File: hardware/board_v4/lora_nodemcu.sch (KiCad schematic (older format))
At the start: 13 parts, among them J1 Solar Panel, J2 LiPo 18650, J6 RF_Shield_ESP-07S, J7 RF_Shield_RFM95

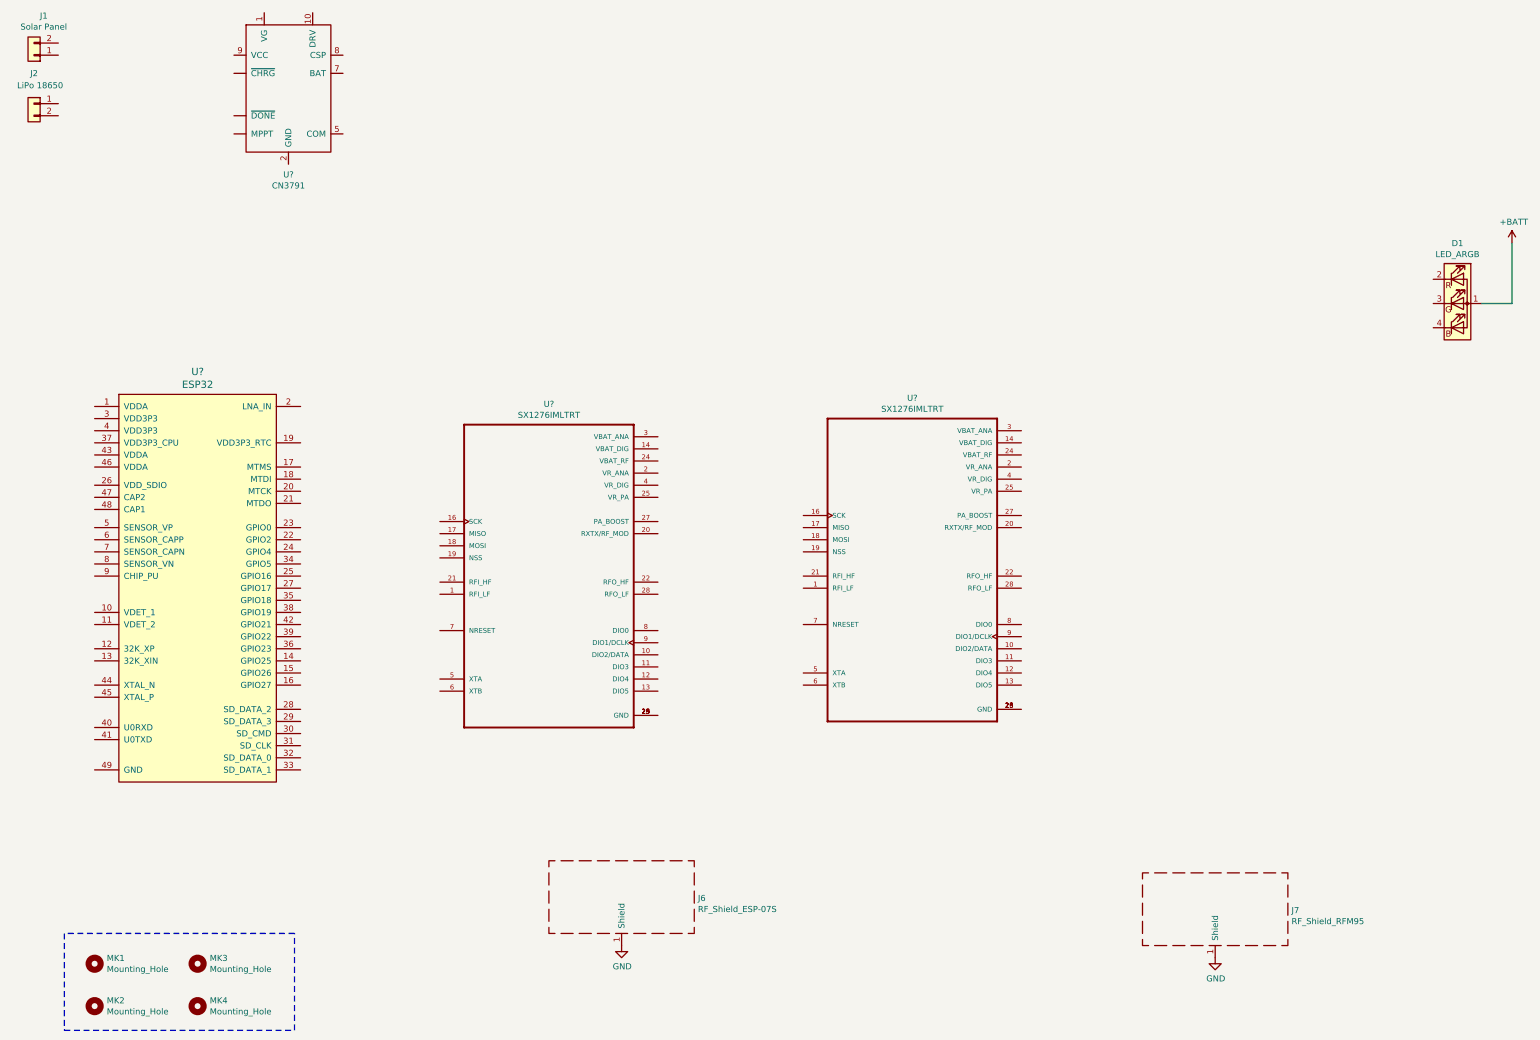
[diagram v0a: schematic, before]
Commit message: adds new ESP32 board
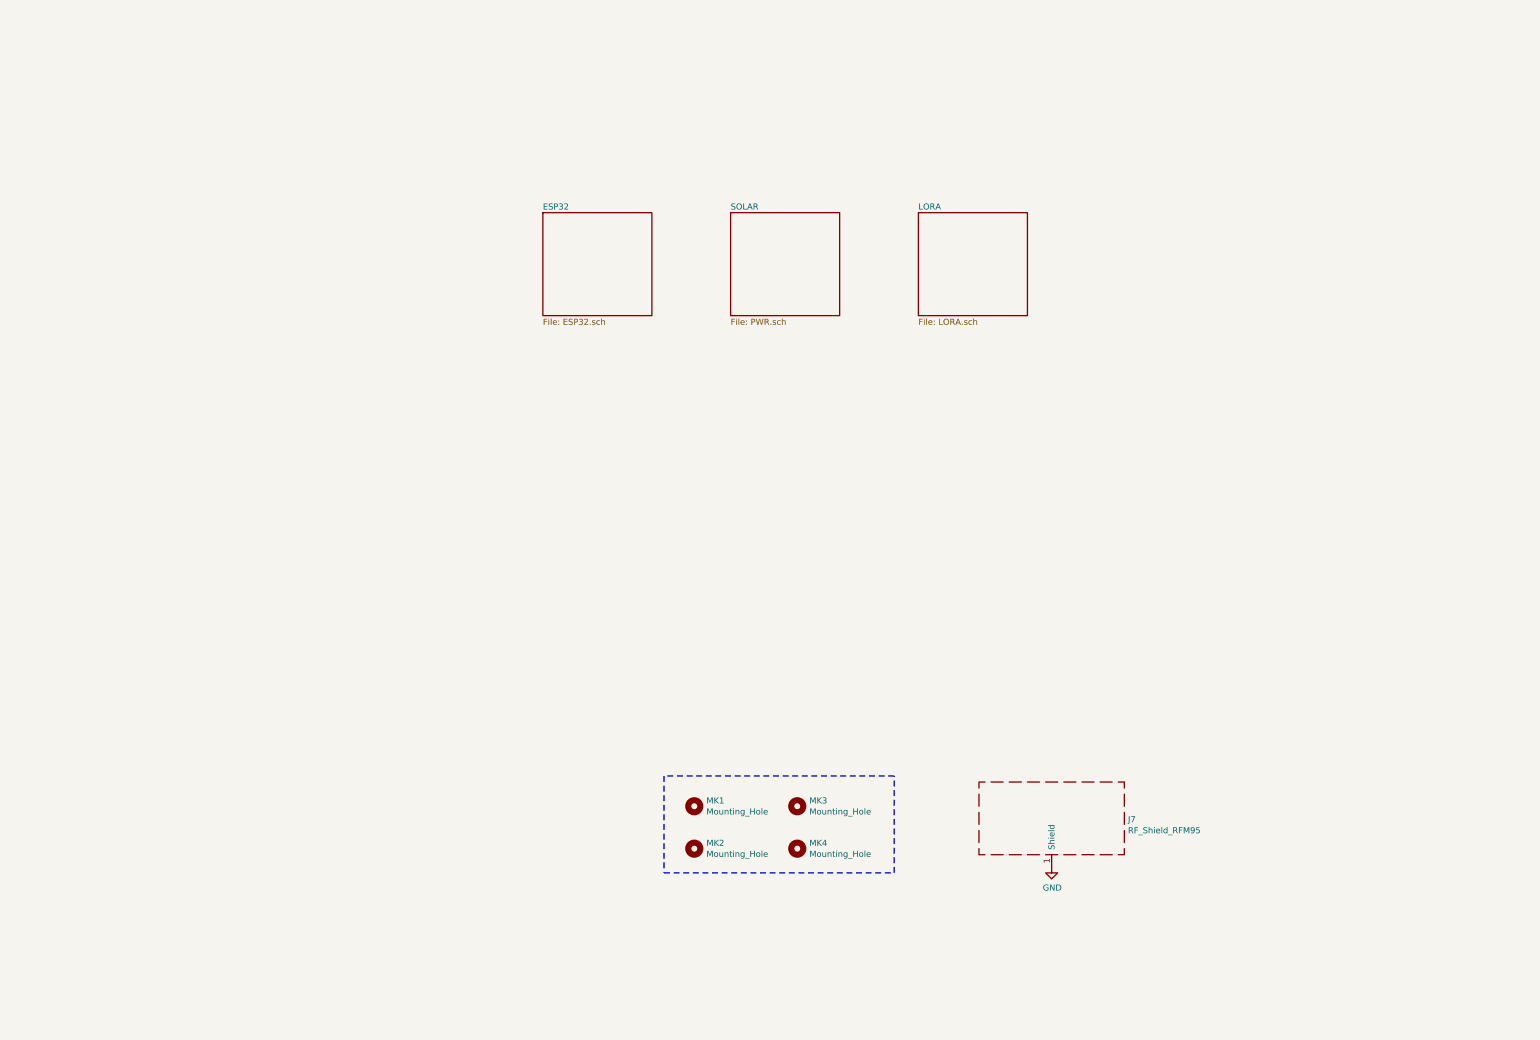
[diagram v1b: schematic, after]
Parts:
- removed D1: LED_ARGB, LED_THT:LED_D5.0mm-4, symbol Device:LED_ARGB
- removed J1: Solar Panel, disaster_radio:solar_panel_conn, symbol Connector_Generic:Conn_01x02
- removed J2: LiPo 18650, Battery:BatteryHolder_MPD_BH-18650-PC2, symbol Connector_Generic:Conn_01x02
- removed J6: RF_Shield_ESP-07S, RF_Shielding:Wuerth_36103305_30x30mm, symbol Device:RF_Shield_One_Piece
- removed U?: CN3791, symbol disaster_radio:CN3791
- removed U?: ESP32, ESP32-footprints-Lib:ESP32, symbol disaster_radio:ESP32
- removed U? (x2): SX1276IMLTRT, QFN65P600X600X100-29N, symbol disaster_radio:SX1276IMLTRT
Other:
- moved on the sheet: J7, MK1, MK2, MK3, MK4
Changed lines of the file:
@@
 EESchema Schematic File Version 4
 LIBS:lora_nodemcu-cache
-EELAYER 26 0
+EELAYER 29 0
 EELAYER END
 $Descr A3 16535 11693
 encoding utf-8
-Sheet 1 1
+Sheet 1 4
 Title ""
 Date ""
@@
 $EndDescr
 $Comp
-L Connector_Generic:Conn_01x02 J2
-U 1 1 5AA4CAA2
-P 1350 1850
-F 0 "J2" H 1350 2100 50  0000 C CNN
-F 1 "LiPo 18650" H 1300 2000 50  0000 C CNN
-F 2 "Battery:BatteryHolder_MPD_BH-18650-PC2" H 1350 1850 50  0001 C CNN
-F 3 "~" H 1350 1850 50  0001 C CNN
-	1    1350 1850
-	-1   0    0    -1
-$EndComp
-$Comp
-L Connector_Generic:Conn_01x02 J1
-U 1 1 5AA4DEE1
-P 1350 1450
-F 0 "J1" H 1270 1125 50  0000 C CNN
-F 1 "Solar Panel" H 1270 1216 50  0000 C CNN
-F 2 "disaster_radio:solar_panel_conn" H 1350 1450 50  0001 C CNN
-F 3 "~" H 1350 1450 50  0001 C CNN
-	1    1350 1450
-	-1   0    0    1
-$EndComp
-$Comp
-L power:+BATT #PWR0125
-U 1 1 5ADE71D1
-P 13550 3000
-F 0 "#PWR0125" H 13550 2850 50  0001 C CNN
-F 1 "+BATT" H 13565 3173 50  0000 C CNN
-F 2 "" H 13550 3000 50  0001 C CNN
-F 3 "" H 13550 3000 50  0001 C CNN
-	1    13550 3000
-	1    0    0    -1
-$EndComp
-Wire Wire Line
-	13550 3000 13550 3500
-$Comp
 L lora_nodemcu-rescue:Mounting_Hole-Mechanical MK1
 U 1 1 5ABC6521
-P 1850 8950
-F 0 "MK1" H 1950 8996 50  0000 L CNN
-F 1 "Mounting_Hole" H 1950 8905 50  0000 L CNN
-F 2 "MountingHole:MountingHole_3.2mm_M3" H 1850 8950 50  0001 C CNN
-F 3 "" H 1850 8950 50  0001 C CNN
-	1    1850 8950
+P 6800 7650
+F 0 "MK1" H 6900 7696 50  0000 L CNN
+F 1 "Mounting_Hole" H 6900 7605 50  0000 L CNN
+F 2 "MountingHole:MountingHole_3.2mm_M3" H 6800 7650 50  0001 C CNN
+F 3 "" H 6800 7650 50  0001 C CNN
+	1    6800 7650
 	1    0    0    -1
 $EndComp
@@
 L lora_nodemcu-rescue:Mounting_Hole-Mechanical MK3
 U 1 1 5ABC68A6
-P 2700 8950
-F 0 "MK3" H 2800 8996 50  0000 L CNN
-F 1 "Mounting_Hole" H 2800 8905 50  0000 L CNN
-F 2 "MountingHole:MountingHole_3.2mm_M3" H 2700 8950 50  0001 C CNN
-F 3 "" H 2700 8950 50  0001 C CNN
-	1    2700 8950
+P 7650 7650
+F 0 "MK3" H 7750 7696 50  0000 L CNN
+F 1 "Mounting_Hole" H 7750 7605 50  0000 L CNN
+F 2 "MountingHole:MountingHole_3.2mm_M3" H 7650 7650 50  0001 C CNN
+F 3 "" H 7650 7650 50  0001 C CNN
+	1    7650 7650
 	1    0    0    -1
 $EndComp
@@
 L lora_nodemcu-rescue:Mounting_Hole-Mechanical MK2
 U 1 1 5ABC6A8E
-P 1850 9300
-F 0 "MK2" H 1950 9346 50  0000 L CNN
-F 1 "Mounting_Hole" H 1950 9255 50  0000 L CNN
-F 2 "MountingHole:MountingHole_3.2mm_M3" H 1850 9300 50  0001 C CNN
-F 3 "" H 1850 9300 50  0001 C CNN
-	1    1850 9300
+P 6800 8000
+F 0 "MK2" H 6900 8046 50  0000 L CNN
+F 1 "Mounting_Hole" H 6900 7955 50  0000 L CNN
+F 2 "MountingHole:MountingHole_3.2mm_M3" H 6800 8000 50  0001 C CNN
+F 3 "" H 6800 8000 50  0001 C CNN
+	1    6800 8000
 	1    0    0    -1
 $EndComp
@@
 L lora_nodemcu-rescue:Mounting_Hole-Mechanical MK4
 U 1 1 5ABC6A95
-P 2700 9300
-F 0 "MK4" H 2800 9346 50  0000 L CNN
-F 1 "Mounting_Hole" H 2800 9255 50  0000 L CNN
-F 2 "MountingHole:MountingHole_3.2mm_M3" H 2700 9300 50  0001 C CNN
-F 3 "" H 2700 9300 50  0001 C CNN
-	1    2700 9300
+P 7650 8000
+F 0 "MK4" H 7750 8046 50  0000 L CNN
+F 1 "Mounting_Hole" H 7750 7955 50  0000 L CNN
+F 2 "MountingHole:MountingHole_3.2mm_M3" H 7650 8000 50  0001 C CNN
+F 3 "" H 7650 8000 50  0001 C CNN
+	1    7650 8000
 	1    0    0    -1
 $EndComp
-$Comp
-L Device:LED_ARGB D1
-U 1 1 5ABCE072
-P 13100 3500
-F 0 "D1" H 13100 3997 50  0000 C CNN
-F 1 "LED_ARGB" H 13100 3906 50  0000 C CNN
-F 2 "LED_THT:LED_D5.0mm-4" H 13100 3450 50  0001 C CNN
-F 3 "~" H 13100 3450 50  0001 C CNN
-	1    13100 3500
-	1    0    0    -1
-$EndComp
-Wire Wire Line
-	13300 3500 13550 3500
 Wire Notes Line
-	1600 8700 1600 9500
+	6550 7400 6550 8200
 Wire Notes Line
-	1600 9500 3500 9500
+	6550 8200 8450 8200
 Wire Notes Line
-	3500 9500 3500 8700
+	8450 8200 8450 7400
 Wire Notes Line
-	3500 8700 1600 8700
-$Comp
-L disaster_radio:CN3791 U?
-U 1 1 5BEC3801
-P 3450 1700
-F 0 "U?" H 3450 964 50  0000 C CNN
-F 1 "CN3791" H 3450 873 50  0000 C CNN
-F 2 "" H 3450 1700 50  0001 C CNN
-F 3 "" H 3450 1700 50  0001 C CNN
-	1    3450 1700
-	1    0    0    -1
-$EndComp
-$Comp
-L disaster_radio:ESP32 U?
-U 1 1 5BEE2399
-P 2700 5900
-F 0 "U?" H 2700 7737 60  0000 C CNN
-F 1 "ESP32" H 2700 7631 60  0000 C CNN
-F 2 "ESP32-footprints-Lib:ESP32" H 2700 4275 60  0001 C CNN
-F 3 "" H 3150 6800 60  0001 C CNN
-	1    2700 5900
-	1    0    0    -1
-$EndComp
-$Comp
-L power:GND #PWR0128
-U 1 1 5AB442E3
-P 6200 8800
-F 0 "#PWR0128" H 6200 8550 50  0001 C CNN
-F 1 "GND" H 6205 8627 50  0000 C CNN
-F 2 "" H 6200 8800 50  0001 C CNN
-F 3 "" H 6200 8800 50  0001 C CNN
-	1    6200 8800
-	1    0    0    -1
-$EndComp
-$Comp
-L Device:RF_Shield_One_Piece J6
-U 1 1 5AB442DC
-P 6200 8400
-F 0 "J6" H 6830 8391 50  0000 L CNN
-F 1 "RF_Shield_ESP-07S" H 6830 8300 50  0000 L CNN
-F 2 "RF_Shielding:Wuerth_36103305_30x30mm" H 6200 8300 50  0001 C CNN
-F 3 "~" H 6200 8300 50  0001 C CNN
-	1    6200 8400
-	1    0    0    -1
-$EndComp
+	8450 7400 6550 7400
 $Comp
 L power:GND #PWR0127
 U 1 1 5AB4404A
-P 11100 8900
-F 0 "#PWR0127" H 11100 8650 50  0001 C CNN
-F 1 "GND" H 11105 8727 50  0000 C CNN
-F 2 "" H 11100 8900 50  0001 C CNN
-F 3 "" H 11100 8900 50  0001 C CNN
-	1    11100 8900
+P 9750 8150
+F 0 "#PWR0127" H 9750 7900 50  0001 C CNN
+F 1 "GND" H 9755 7977 50  0000 C CNN
+F 2 "" H 9750 8150 50  0001 C CNN
+F 3 "" H 9750 8150 50  0001 C CNN
+	1    9750 8150
 	1    0    0    -1
 $EndComp
@@
 L Device:RF_Shield_One_Piece J7
 U 1 1 5AB43EB6
-P 11100 8500
-F 0 "J7" H 11730 8491 50  0000 L CNN
-F 1 "RF_Shield_RFM95" H 11730 8400 50  0000 L CNN
-F 2 "RF_Shielding:Wuerth_36103305_30x30mm" H 11100 8400 50  0001 C CNN
-F 3 "~" H 11100 8400 50  0001 C CNN
-	1    11100 8500
+P 9750 7750
+F 0 "J7" H 10380 7741 50  0000 L CNN
+F 1 "RF_Shield_RFM95" H 10380 7650 50  0000 L CNN
+F 2 "RF_Shielding:Wuerth_36103305_30x30mm" H 9750 7650 50  0001 C CNN
+F 3 "~" H 9750 7650 50  0001 C CNN
+	1    9750 7750
 	1    0    0    -1
 $EndComp
-$Comp
-L disaster_radio:SX1276IMLTRT U?
-U 1 1 5BEE32F7
-P 5600 5800
-F 0 "U?" H 5600 7270 50  0000 C CNN
-F 1 "SX1276IMLTRT" H 5600 7179 50  0000 C CNN
-F 2 "QFN65P600X600X100-29N" H 5600 5800 50  0001 L BNN
-F 3 "SX1276IMLTRT" H 5600 5800 50  0001 L BNN
-F 4 "None" H 5600 5800 50  0001 L BNN "Field4"
-F 5 "Rf Ism Transceiver Fsk/gfsk/gmsk/msk/ook 3.3V Automotive 28-PIN QFN Ep T/r" H 5600 5800 50  0001 L BNN "Field5"
-F 6 "Unavailable" H 5600 5800 50  0001 L BNN "Field6"
-F 7 "VQFN-28 Semtech" H 5600 5800 50  0001 L BNN "Field7"
-F 8 "Semtech Corporation" H 5600 5800 50  0001 L BNN "Field8"
-	1    5600 5800
-	1    0    0    -1
-$EndComp
-$Comp
-L disaster_radio:SX1276IMLTRT U?
-U 1 1 5BEE3441
-P 8600 5750
-F 0 "U?" H 8600 7220 50  0000 C CNN
-F 1 "SX1276IMLTRT" H 8600 7129 50  0000 C CNN
-F 2 "QFN65P600X600X100-29N" H 8600 5750 50  0001 L BNN
-F 3 "SX1276IMLTRT" H 8600 5750 50  0001 L BNN
-F 4 "None" H 8600 5750 50  0001 L BNN "Field4"
-F 5 "Rf Ism Transceiver Fsk/gfsk/gmsk/msk/ook 3.3V Automotive 28-PIN QFN Ep T/r" H 8600 5750 50  0001 L BNN "Field5"
-F 6 "Unavailable" H 8600 5750 50  0001 L BNN "Field6"
-F 7 "VQFN-28 Semtech" H 8600 5750 50  0001 L BNN "Field7"
-F 8 "Semtech Corporation" H 8600 5750 50  0001 L BNN "Field8"
-	1    8600 5750
-	1    0    0    -1
-$EndComp
+$Sheet
+S 5550 2750 900  850
+U 5C0025BF
+F0 "ESP32" 50
+F1 "ESP32.sch" 50
+$EndSheet
+$Sheet
+S 7100 2750 900  850
+U 5BFE367E
+F0 "SOLAR" 50
+F1 "PWR.sch" 50
+$EndSheet
+$Sheet
+S 8650 2750 900  850
+U 5BFE48D4
+F0 "LORA" 50
+F1 "LORA.sch" 50
+$EndSheet
 $EndSCHEMATC
